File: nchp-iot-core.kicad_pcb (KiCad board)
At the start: 2 copper layers, 34 x 61.2 mm, 49 parts, among them P1 USB, P10 CONN_01X01, P11 CONN_01X01, P2 CONN_01X02, P3 CONN_01X16, P4 CONN_01X04, P5 CONN_01X16, P6 CONN_01X03, P7 CONN_01X03, P8 CONN_01X01, P9 CONN_01X01, SW1 RST, SW2 SW_PUSH_SMALL_H, U1 LP2985LV, U2 STM32F103C8Tx, U3 ESP-07v2, Y1 8MHz

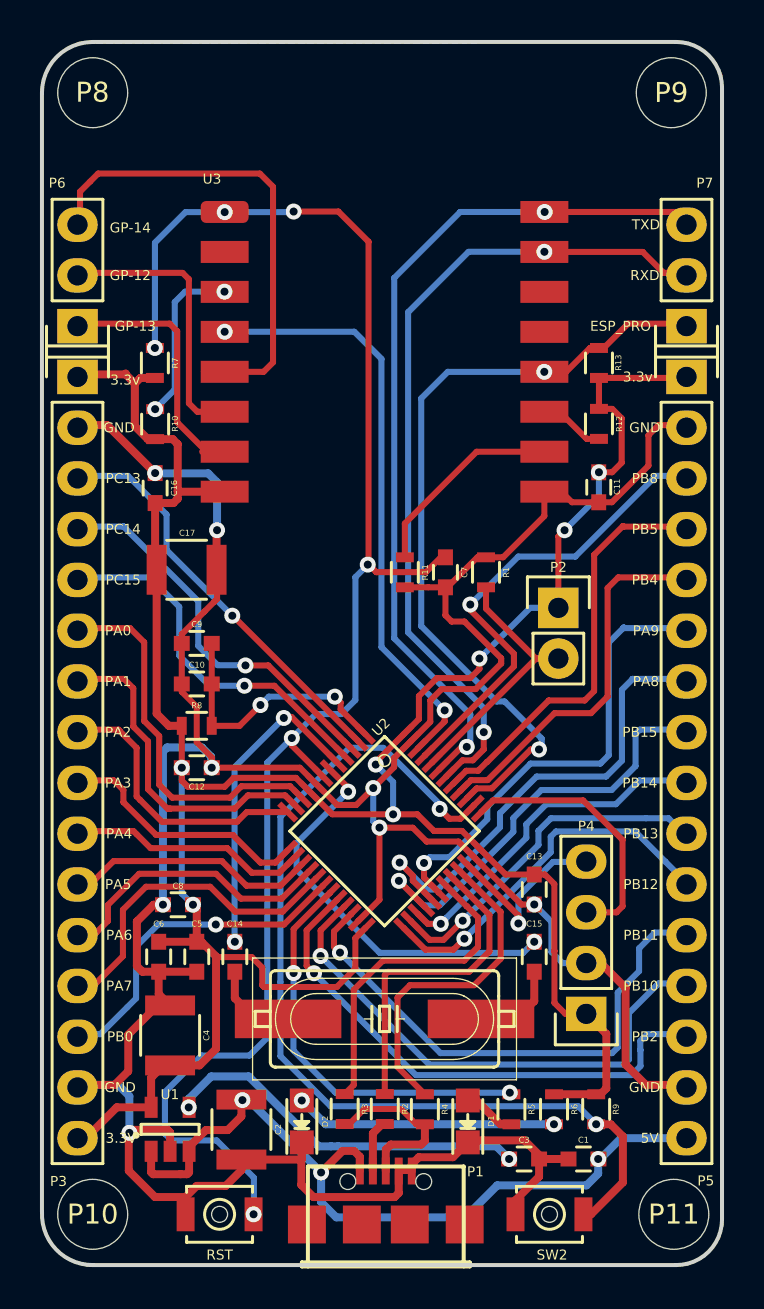
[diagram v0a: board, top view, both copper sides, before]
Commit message: Confirm PIN 1 of ESP8266 & STM32
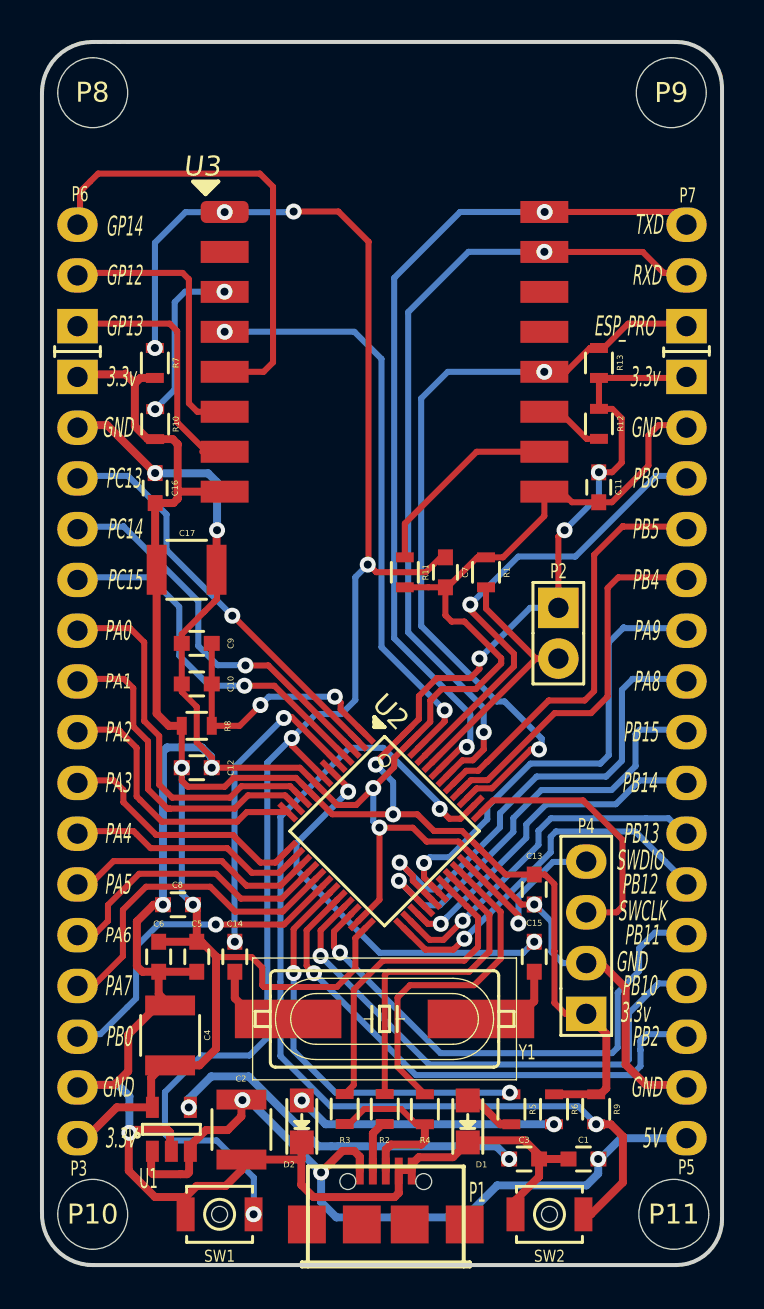
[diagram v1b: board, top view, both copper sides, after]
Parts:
- SW1: value RST -> SW1
- moved U1 0.06 mm to (111.4, 129.1)
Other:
- board text added: "GP12"
- board text added: "GP13"
- board text added: "GP14"
- board text added: "SWCLK"
- board text added: "SWDIO"
- board text removed: "GP-12"
- board text removed: "GP-13"
- board text removed: "GP-14"
